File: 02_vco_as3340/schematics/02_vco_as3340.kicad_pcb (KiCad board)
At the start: 2 copper layers, 90 x 180 mm, 87 parts, among them J1 EURORACK, J10 Triangle Out, J11 Sine Out, J12 1V/O Thru, J2 1V/O IN, J3 Positive Hard Sync IN, J4 Negative Hard Sync IN, J5 Soft Sync In, J6 FM IN, J7 PWM CV IN, J8 Square Out, J9 Sawtooth Out, Q1 2N3904, Q2 2N3904, U1 TL074, U2 AS3340, U3 TL072

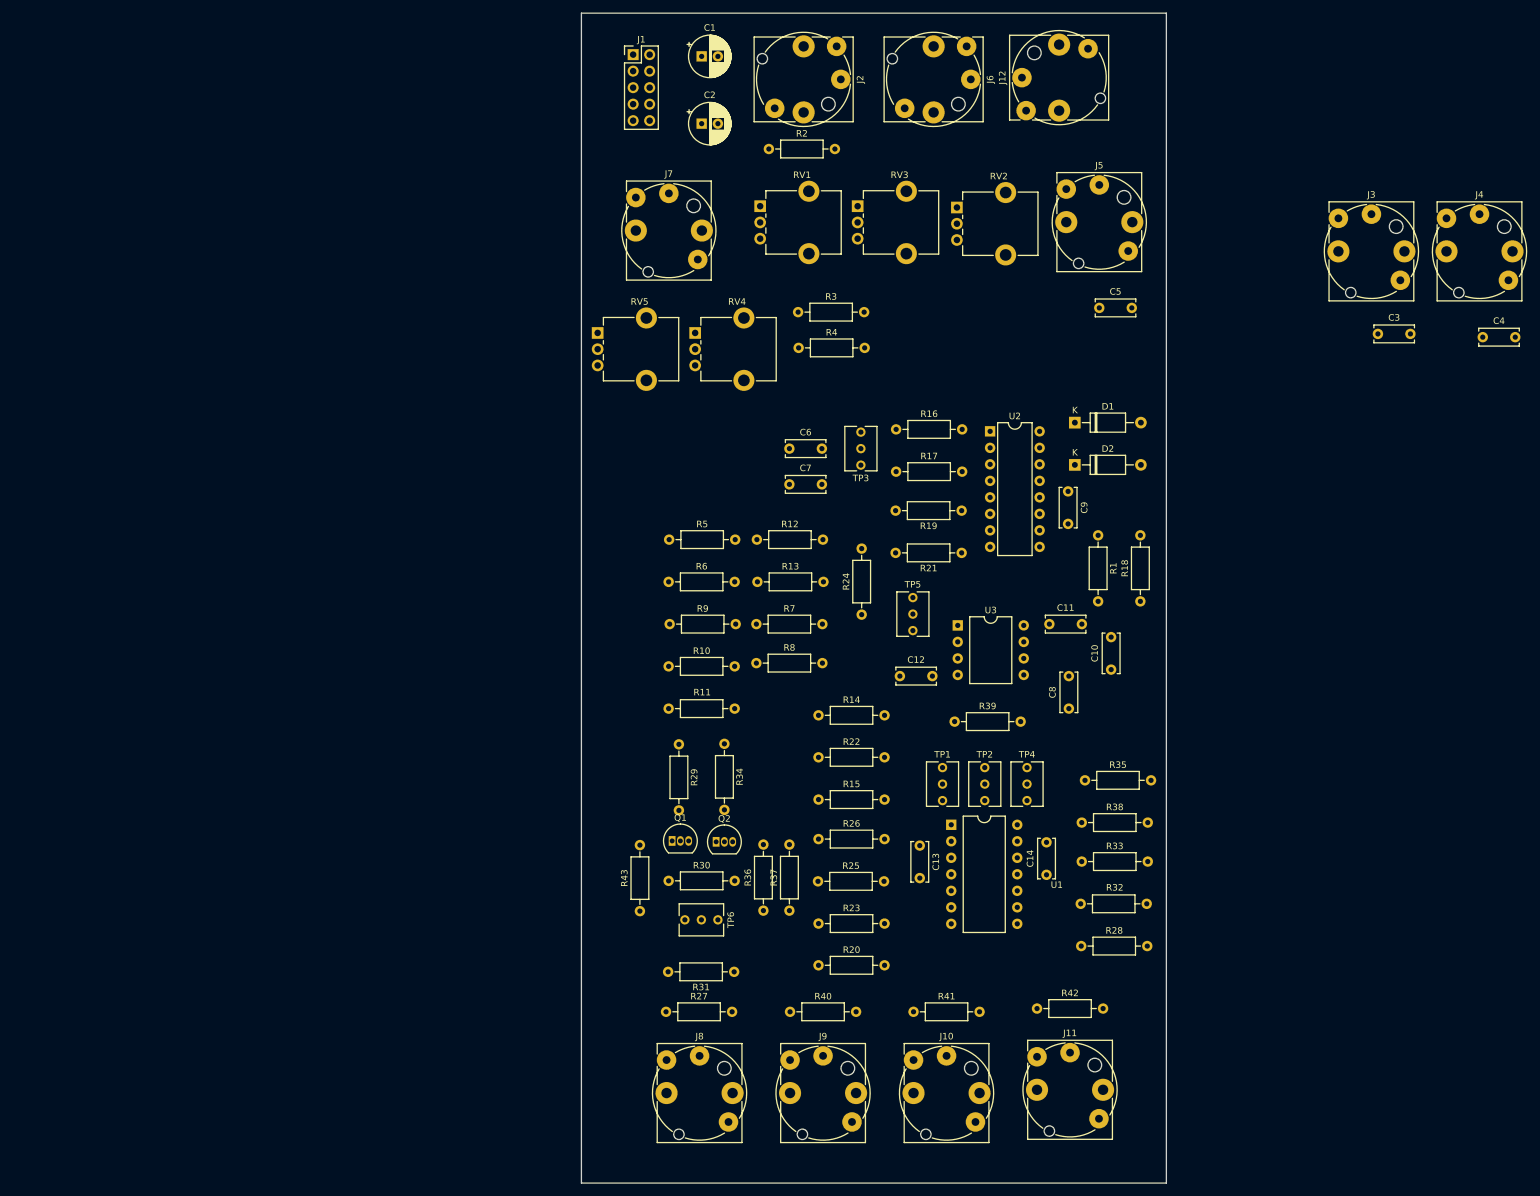
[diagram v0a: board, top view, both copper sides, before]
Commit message: fixed triangle output
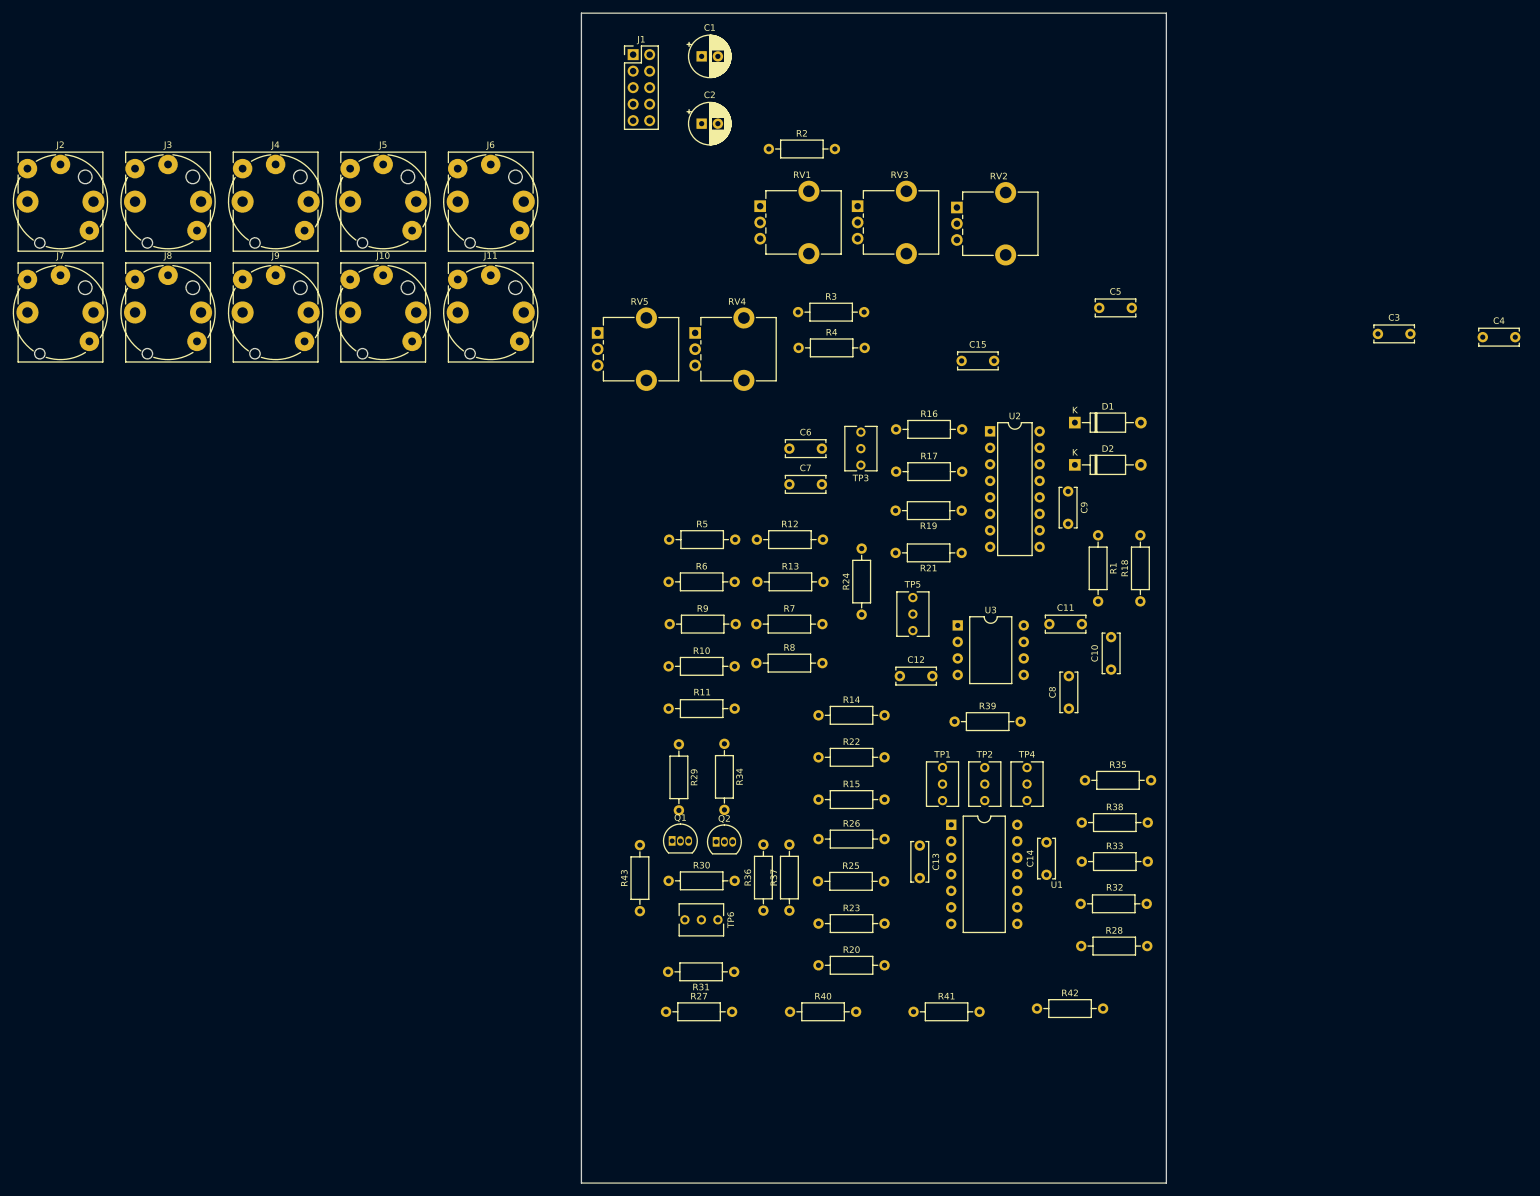
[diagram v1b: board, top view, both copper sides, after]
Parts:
- removed J12: 1V/O Thru, Connector_Audio:Jack_6.35mm_Neutrik_NJ5FD-V_Vertical
- added C15: 100nF, Capacitor_THT:C_Disc_D6.0mm_W2.5mm_P5.00mm, F.Cu at (133.0, 73.0)
- J1: value EURORACK -> Conn_02x05_Odd_Even
- moved J4 185.4 mm to (27.4, 42.8)
- moved J3 185.3 mm to (10.9, 42.8)
- moved J11 149.2 mm to (60.5, 59.8)
- moved J10 148.1 mm to (44.0, 59.8)
- moved J9 146.7 mm to (27.4, 59.8)
- moved J8 145.3 mm to (10.9, 59.8)
- moved J2 120.8 mm to (-5.65, 42.8), turned to 0 degrees
- moved J5 110.2 mm to (44.0, 42.8)
- moved J7 94.4 mm to (-5.65, 59.8)
- moved J6 75.0 mm to (60.5, 42.8), turned to 0 degrees
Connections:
- net 1V/O THRU renamed Net-(J2-PadT)
- Q2 pad 3: Net-(Q1-C) -> Net-(Q2-C)
- R34 pad 2: Net-(Q1-C) -> Net-(Q2-C)
- R37 pad 2: Net-(Q1-C) -> Net-(Q2-C)
- R41 pad 1: Net-(U3A--) -> Net-(U3A-+)
- U3 pad 5: Net-(Q1-C) -> Net-(Q2-C)

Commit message: added PCB for 02
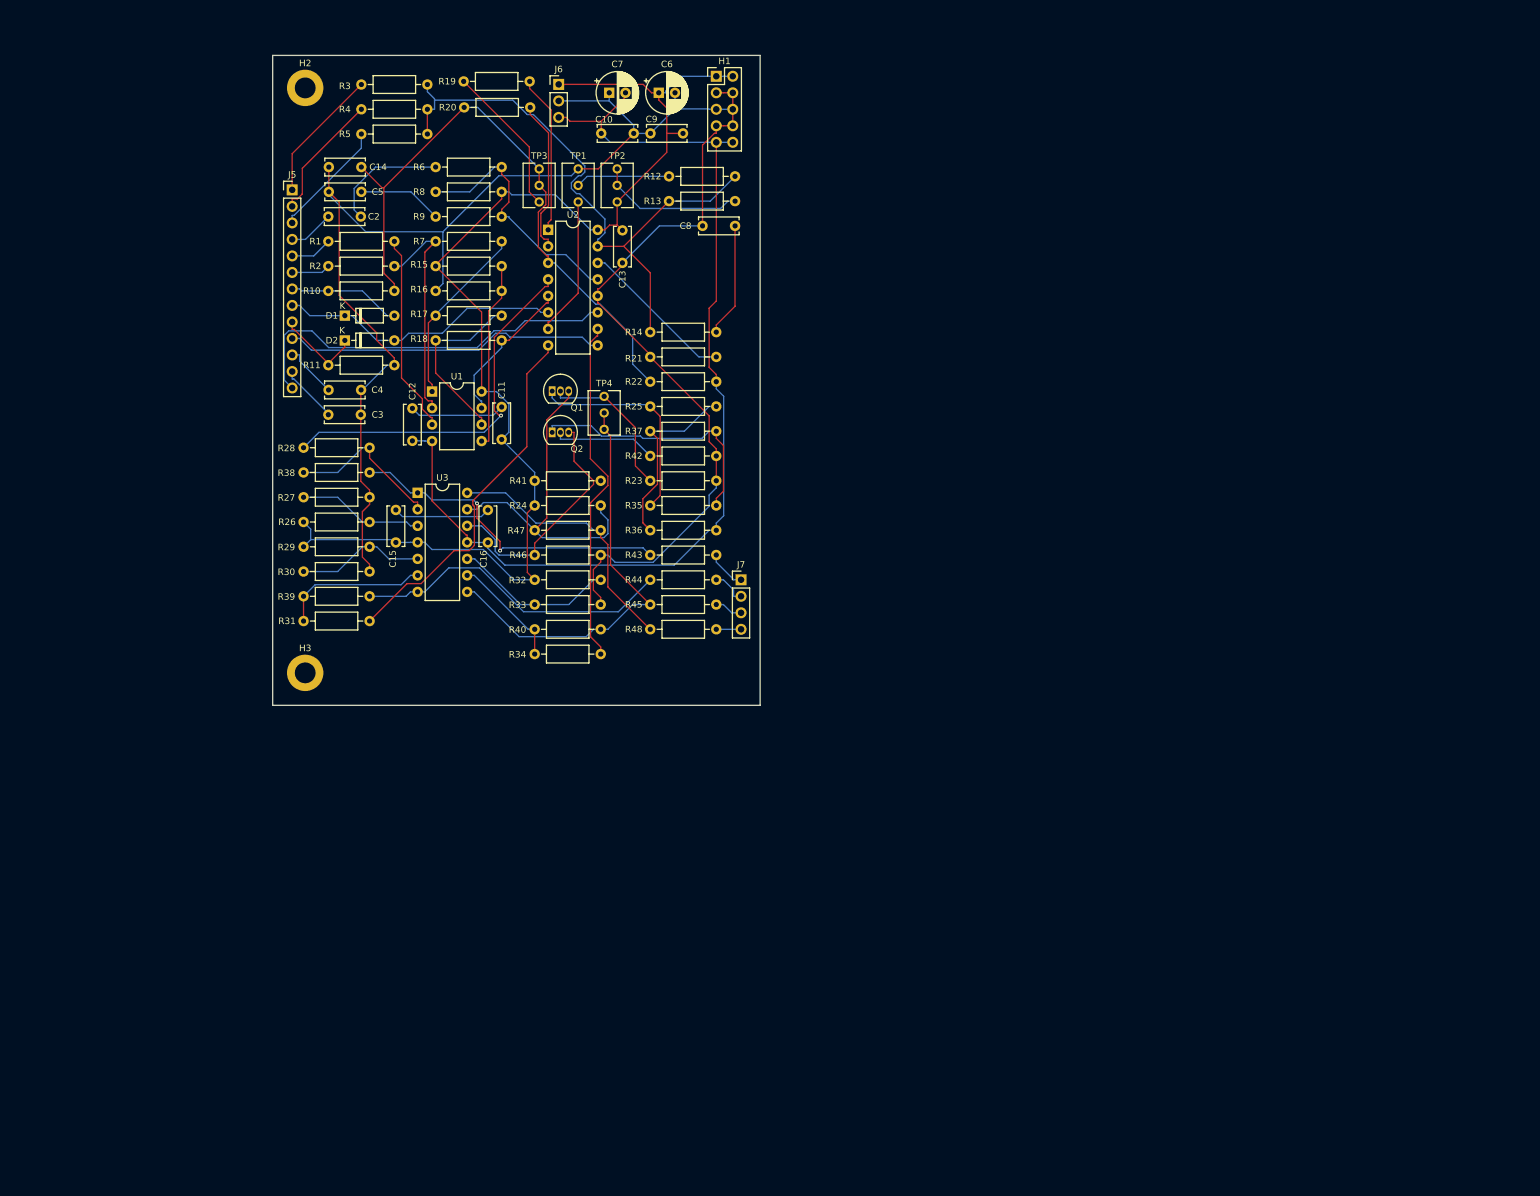
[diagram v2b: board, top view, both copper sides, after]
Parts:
- removed C1: 47uF, Capacitor_THT:CP_Radial_D6.3mm_P2.50mm
- removed J1: Conn_02x05_Odd_Even, Connector_PinHeader_2.54mm:PinHeader_2x05_P2.54mm_Vertical
- removed J10: Triangle Out, Connector_Audio:Jack_6.35mm_Neutrik_NJ5FD-V_Vertical
- removed J11: Sine Out, Connector_Audio:Jack_6.35mm_Neutrik_NJ5FD-V_Vertical
- removed J2: 1V/O IN, Connector_Audio:Jack_6.35mm_Neutrik_NJ5FD-V_Vertical
- removed J3: Positive Hard Sync IN, Connector_Audio:Jack_6.35mm_Neutrik_NJ5FD-V_Vertical
- removed J4: Negative Hard Sync IN, Connector_Audio:Jack_6.35mm_Neutrik_NJ5FD-V_Vertical
- removed J8: Square Out, Connector_Audio:Jack_6.35mm_Neutrik_NJ5FD-V_Vertical
- removed J9: Sawtooth Out, Connector_Audio:Jack_6.35mm_Neutrik_NJ5FD-V_Vertical
- removed RV1, RV2, RV3, RV4, RV5: 100k, Potentiometer_THT:Potentiometer_Alpha_RD901F-40-00D_Single_Vertical_CircularHoles
- removed TP5: 100k, Potentiometer_THT:Potentiometer_Vishay_T73XW_Horizontal
- removed TP6: 50k, Potentiometer_THT:Potentiometer_Vishay_T73XW_Horizontal
- added C16: 100nF, Capacitor_THT:C_Disc_D6.0mm_W2.5mm_P5.00mm, F.Cu at (60.1, 100.9)
- added H1: Eurorack 10 pin header, Connector_PinHeader_2.54mm:PinHeader_2x05_P2.54mm_Vertical, F.Cu at (95.2, 29.2)
- added H2: MountingHole, MountingHole:MountingHole_3.2mm_M3_DIN965_Pad, F.Cu at (32.0, 31.0)
- added H3: MountingHole, MountingHole:MountingHole_3.2mm_M3_DIN965_Pad, F.Cu at (32.0, 121.0)
- added R44: 1k, Resistor_THT:R_Axial_DIN0207_L6.3mm_D2.5mm_P10.16mm_Horizontal, F.Cu at (85.1, 106.7)
- added R45: 1k, Resistor_THT:R_Axial_DIN0207_L6.3mm_D2.5mm_P10.16mm_Horizontal, F.Cu at (85.1, 110.5)
- added R46: 24k, Resistor_THT:R_Axial_DIN0207_L6.3mm_D2.5mm_P10.16mm_Horizontal, F.Cu at (67.3, 102.9)
- added R47: 24k, Resistor_THT:R_Axial_DIN0207_L6.3mm_D2.5mm_P10.16mm_Horizontal, F.Cu at (67.3, 99.1)
- added R48: 1k, Resistor_THT:R_Axial_DIN0207_L6.3mm_D2.5mm_P10.16mm_Horizontal, F.Cu at (85.1, 114.3)
- C2: value 47uF -> 100nF; footprint Capacitor_THT:CP_Radial_D6.3mm_P2.50mm -> Capacitor_THT:C_Disc_D6.0mm_W2.5mm_P5.00mm
- C3, C5: value 1nF -> 10nF
- C4: value 1nF -> 820pF
- C6, C7: value 10nF -> 47uF; footprint Capacitor_THT:C_Disc_D6.0mm_W2.5mm_P5.00mm -> Capacitor_THT:CP_Radial_D6.3mm_P2.50mm
- C9: value 1nF -> 100nF
- D1, D2: footprint Diode_THT:D_A-405_P10.16mm_Horizontal -> Diode_THT:D_DO-35_SOD27_P7.62mm_Horizontal
- J5: value Soft Sync In -> inputs; footprint Connector_Audio:Jack_6.35mm_Neutrik_NJ5FD-V_Vertical -> Connector_PinHeader_2.54mm:PinHeader_1x13_P2.54mm_Vertical
- J6: value FM IN -> Panel Power; footprint Connector_Audio:Jack_6.35mm_Neutrik_NJ5FD-V_Vertical -> Connector_PinHeader_2.54mm:PinHeader_1x03_P2.54mm_Vertical
- J7: value PWM CV IN -> Outputs; footprint Connector_Audio:Jack_6.35mm_Neutrik_NJ5FD-V_Vertical -> Connector_PinHeader_2.54mm:PinHeader_1x04_P2.54mm_Vertical
- Q1, Q2: value 2N3904 -> BC547C
- R1: value 1M -> 100k
- R10: value 200k -> 10k
- R11: value 470R -> 10k
- R12: value 47k -> 1M
- R13: value 220k -> 270k
- R14: value 100k -> 470R
- R15: value 47k -> 220k
- R16: value 24k -> 47k
- R17: value 5k6 -> 220k
- R18: value 1k8 -> 47k
- R19: value 910R -> 24k
- R20: value 33k -> 5k6
- R21: value 100k -> 1k8
- R22: value 100k -> 680R
- R23: value 82k -> 2k2
- R24: value 33k -> 10k
- R25: value 150k -> 47k
- R26: value 15k -> 100k
- R27: value 1k -> 27k
- R28: value 82k -> 100k
- R29: value 10k -> 120k
- R3: value 300k -> 100k
- R30: value 390R -> 27k
- R31: value 18k -> 100k
- R32: value 100k -> 150k
- R33: value 22k -> 20k
- R34: value 10k -> 33k
- R35: value 100k -> 390R
- R36: value 2k2 -> 33k
- R37: value 10k -> 47k
- R38: value 100k -> 82k
- R39: value 15k -> 120k
- R4: value 3M3 -> 300k
- R40: value 1k -> 82k
- R41: value 1k -> 10k
- R42: value 1k -> 2k2
- R43: value 2k2 -> 1k
- R5: value 1M5 -> 3M3
- R6: value 470R -> 1M
- R7: value 10k -> 100k
- R8: value 10k -> 1M2
- R9: value 1M -> 470R
- TP4: value 10k -> 50k
- U1: value TL074 -> TL072; footprint Package_DIP:DIP-14_W10.16mm -> Package_DIP:DIP-8_W7.62mm
- U3: value TL072 -> TL074; footprint Package_DIP:DIP-8_W10.16mm -> Package_DIP:DIP-14_W7.62mm
- moved C4 172.8 mm to (40.6, 77.5), turned to 180 degrees
- moved C3 162.0 mm to (35.6, 81.3)
- moved C14 155.1 mm to (35.6, 43.2), turned to 0 degrees
- moved R20 142.8 mm to (56.5, 34.0)
- moved R28 142.1 mm to (31.8, 86.4)
- moved R38 131.3 mm to (31.8, 90.2)
- moved R1 126.8 mm to (35.6, 54.6), turned to 0 degrees
- moved C5 119.9 mm to (35.6, 47.0)
- moved R18 115.6 mm to (52.1, 69.8), turned to 0 degrees
- moved J7 114.7 mm to (99.1, 106.7)
- moved D2 113.9 mm to (38.1, 69.8)
- moved C10 113.8 mm to (77.5, 38.0), turned to 0 degrees
- moved D1 113.5 mm to (38.1, 66.0)
- moved TP2 108.1 mm to (80.0, 43.5)
- moved TP1 107.8 mm to (74.0, 43.5)
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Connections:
- C10 pad 1: GNDREF -> -12V
- C10 pad 2: +12V -> GND
- C11 pad 1: GNDREF -> Net-(C11-Pad1)
- C12 pad 2: GNDREF -> Net-(C11-Pad1)
- C13 pad 1: GNDREF -> GND
- C14 pad 1: -12V -> GND
- C14 pad 2: GNDREF -> Net-(U2-VEE)
- C15 pad 1: GNDREF -> Net-(C15-Pad1)
- C15 pad 2: Net-(U2-VEE) -> +12V
- C2 pad 1: GNDREF -> Net-(C2-Pad1)
- C2 pad 2: -12V -> /PCB/FM
- C3 pad 1: Net-(C3-Pad1) -> /PCB/Mode LFO
- C3 pad 2: Net-(D1-A) -> GND
- C4 pad 1: Net-(C4-Pad1) -> GND
- C4 pad 2: Net-(D2-K) -> /PCB/Mode VCO
- C5 pad 1: Net-(C5-Pad1) -> GND
- C5 pad 2: Net-(U2-VSSI) -> Net-(C5-Pad2)
- C6 pad 1: Net-(C6-Pad1) -> +12V
- C6 pad 2: Net-(C6-Pad2) -> GND
- C7 pad 1: GNDREF -> GND
- C7 pad 2: Net-(C7-Pad2) -> -12V
- C8 pad 2: GNDREF -> GND
- C9 pad 1: GNDREF -> GND
- C9 pad 2: Net-(U2-CAP) -> +12V
- D1 pad 1: Net-(D1-K) -> /PCB/Hard Sync
- D1 pad 2: Net-(D1-A) -> /PCB/Positive Hard Sync
- D2 pad 1: Net-(D2-K) -> /PCB/Negative Hard Sync
- D2 pad 2: Net-(D1-K) -> /PCB/Hard Sync
- R1 pad 1: Net-(C6-Pad1) -> /PCB/PWM Offset
- R1 pad 2: Net-(U2-VLFI) -> Net-(U1A-+)
- R10 pad 1: Net-(U2-VFCI) -> /PCB/Positive Hard Sync
- R10 pad 2: Net-(R10-Pad2) -> Net-(U2-VEE)
- R11 pad 1: Net-(U2-VFCI) -> /PCB/Negative Hard Sync
- R11 pad 2: Net-(C8-Pad1) -> GND
- R12 pad 1: Net-(R12-Pad1) -> Net-(U2-VFCI)
- R12 pad 2: +12V -> Net-(R12-Pad2)
- R13 pad 1: Net-(R13-Pad1) -> Net-(U2-VFCI)
- R13 pad 2: -12V -> Net-(R13-Pad2)
- R14 pad 1: Net-(R14-Pad1) -> Net-(U2-VFCI)
- R14 pad 2: Net-(U1A--) -> Net-(C8-Pad1)
- R15 pad 1: Net-(U1A--) -> +12V
- R15 pad 2: Net-(U2-VPWM) -> Net-(U1B-+)
- R16 pad 1: Net-(R16-Pad1) -> GND
- R16 pad 2: Net-(U2-SCALE1) -> Net-(U1B-+)
- R17 pad 1: Net-(U2-VEE) -> Net-(R17-Pad1)
- R17 pad 2: Net-(U2-SCALE2) -> Net-(U1B--)
- R18 pad 1: GNDREF -> Net-(U1B--)
- R18 pad 2: Net-(U2-VS) -> Net-(U2-VPWM)
- R19 pad 1: Net-(U2-VEE) -> Net-(R19-Pad1)
- R19 pad 2: -12V -> Net-(U2-SCALE1)
- R2 pad 1: Net-(J2-PadT) -> /PCB/PWM CV
- R2 pad 2: Net-(U2-VFCI) -> Net-(U1A--)
- R20 pad 1: Net-(U1B-+) -> Net-(U2-VEE)
- R20 pad 2: GNDREF -> Net-(U2-SCALE2)
- R21 pad 1: Net-(U2-VP) -> GND
- R21 pad 2: Net-(U1B--) -> Net-(U2-VS)
- R22 pad 1: +12V -> Net-(U2-VEE)
- R22 pad 2: Net-(U1B-+) -> -12V
- R23 pad 1: Net-(U1B--) -> Net-(Q1-B)
- R23 pad 2: Net-(R23-Pad2) -> GND
- R24 pad 1: Net-(U1C--) -> +12V
- R24 pad 2: Net-(U2-VTO) -> Net-(Q1-C)
- R25 pad 1: +12V -> Net-(Q1-E)
- R25 pad 2: Net-(U1C-+) -> Net-(R25-Pad2)
- R26 pad 1: Net-(R26-Pad1) -> +12V
- R26 pad 2: GNDREF -> Net-(U3A-+)
- R27 pad 1: Net-(R23-Pad2) -> Net-(U3A-+)
- R27 pad 2: Net-(J8-PadT) -> GND
- R28 pad 1: Net-(U1C--) -> Net-(U2-VP)
- R28 pad 2: Net-(U3A-+) -> Net-(U3A--)
- R29 pad 2: Net-(Q1-C) -> Net-(U3B-+)
- R3 pad 1: Net-(R3-Pad1) -> /PCB/1V/O
- R30 pad 1: Net-(Q1-E) -> Net-(U3B-+)
- R30 pad 2: Net-(Q2-E) -> GND
- R31 pad 1: Net-(R31-Pad1) -> Net-(U2-VSO)
- R31 pad 2: -12V -> Net-(U3B--)
- R32 pad 1: Net-(U2-VSO) -> +12V
- R32 pad 2: Net-(U1D--) -> Net-(U3C-+)
- R33 pad 1: Net-(U1D-+) -> Net-(U3C-+)
- R33 pad 2: GNDREF -> GND
- R34 pad 1: +12V -> Net-(U3C--)
- R34 pad 2: Net-(Q2-C) -> Net-(U2-VTO)
- R35 pad 1: +12V -> Net-(Q1-E)
- R35 pad 2: Net-(U1D-+) -> Net-(Q2-E)
- R36 pad 1: GNDREF -> Net-(R25-Pad2)
- R36 pad 2: Net-(Q2-B) -> -12V
- R37 pad 1: GNDREF -> Net-(R25-Pad2)
- R37 pad 2: Net-(Q2-C) -> Net-(Q2-E)
- R38 pad 1: Net-(U1D--) -> Net-(U3A--)
- R39 pad 1: Net-(Q1-C) -> Net-(U3B--)
- R4 pad 1: Net-(R4-Pad1) -> /PCB/Coarse Tune
- R40 pad 1: Net-(R38-Pad2) -> Net-(U3C--)
- R40 pad 2: Net-(J9-PadT) -> Net-(R40-Pad2)
- R41 pad 1: Net-(U3A-+) -> +12V
- R41 pad 2: Net-(J10-PadT) -> Net-(Q2-C)
- R42 pad 1: Net-(R39-Pad2) -> Net-(Q2-B)
- R42 pad 2: Net-(J11-PadT) -> GND
- R43 pad 1: GNDREF -> Net-(R38-Pad2)
- R43 pad 2: Net-(Q1-B) -> /PCB/Square
- R5 pad 1: +12V -> /PCB/Fine Tune
- R5 pad 2: Net-(U2-VLFI) -> Net-(U2-VFCI)
- R6 pad 1: Net-(U2-VLFI) -> Net-(C2-Pad1)
- R6 pad 2: Net-(C7-Pad2) -> Net-(U2-VLFI)
- R7 pad 1: Net-(D1-A) -> Net-(U1A--)
- R7 pad 2: Net-(U2-VEE) -> Net-(R17-Pad1)
- R8 pad 1: Net-(D2-K) -> Net-(U2-VLFI)
- R8 pad 2: GNDREF -> +12V
- R9 pad 1: Net-(U2-VFCI) -> Net-(C5-Pad2)
- R9 pad 2: Net-(R9-Pad2) -> Net-(U2-VLFI)
- TP1 pad 1: GNDREF -> GND
- TP1 pad 2: Net-(R9-Pad2) -> Net-(R12-Pad2)
- TP2 pad 1: Net-(R10-Pad2) -> Net-(R13-Pad2)
- TP2 pad 2: Net-(R10-Pad2) -> Net-(R13-Pad2)
- TP3 pad 3: Net-(R16-Pad1) -> Net-(R19-Pad1)
- TP4 pad 1: Net-(R26-Pad1) -> Net-(Q1-B)
- TP4 pad 2: Net-(U1C-+) -> Net-(R40-Pad2)
- TP4 pad 3: Net-(U1C-+) -> Net-(R40-Pad2)
- U1 pad 1: Net-(U2-VPWM) -> Net-(R17-Pad1)
- U1 pad 4: +12V -> -12V
- U1 pad 7: Net-(R23-Pad2) -> Net-(U2-VPWM)
- U1 pad 8: Net-(U3A-+) -> +12V
- U2 pad 11: Net-(U2-CAP) -> /PCB/Mode
- U2 pad 12: GNDREF -> GND
- U2 pad 6: Net-(D1-K) -> /PCB/Hard Sync
- U2 pad 9: Net-(U2-VSSI) -> /PCB/Soft Sync
- U3 pad 1: Net-(U3A--) -> Net-(R38-Pad2)
- U3 pad 4: -12V -> +12V
- U3 pad 5: Net-(Q2-C) -> Net-(U3B-+)
- U3 pad 6: Net-(Q1-C) -> Net-(U3B--)
- U3 pad 8: +12V -> Net-(R40-Pad2)
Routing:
- net GND: track 0.00 -> 289.1 mm
- net +12V: track 0.00 -> 191.9 mm
- net -12V: track 0.00 -> 160.4 mm
- net Net-(U2-VEE): track 0.00 -> 96.2 mm
- net Net-(U2-VFCI): track 0.00 -> 93.4 mm
- net Net-(R40-Pad2): track 0.00 -> 65.5 mm
- net /PCB/Mode: track 0.00 -> 60.4 mm
- net Net-(U2-VP): track 0.00 -> 57.7 mm, vias 0 -> 1
- net Net-(U2-VSO): track 0.00 -> 56.6 mm
- net Net-(U2-VTO): track 0.00 -> 53.4 mm
- net Net-(Q1-C): track 0.00 -> 52.9 mm
- net Net-(R38-Pad2): track 0.00 -> 51.0 mm, vias 0 -> 2
- net Net-(R39-Pad2): track 0.00 -> 49.8 mm
- net /PCB/Soft Sync: track 0.00 -> 49.6 mm
- net /PCB/Hard Sync: track 0.00 -> 43.9 mm
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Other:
- board size 90 x 180 mm -> 75 x 100 mm
